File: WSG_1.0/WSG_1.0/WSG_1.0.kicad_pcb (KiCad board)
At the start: 4 copper layers, 53.8 x 34.1 mm, 100 parts, among them J1 Conn_01x10, J2 USB_C_Receptacle_USB2.0_16P, J4 Conn_01x02, SW1 SW_Push, SW2 SW_Push, U1 ADS131A04IPBSR, U10 TPS22916CYFPR, U11 W25N04KVZEIR, U12 USBLC6-2SC6, U13 ESP32-S3-MINI-1-N8, U14 TPD4E1U06DBVR, U2 DAC60501ZDGSR, U3 INA827AIDGKR, U4 INA827AIDGKR, U5 INA827AIDGKR, U6 TMP235A2DBZR, U7 BQ25180YBGR, U8 TPS63802DLAR, U9 TPS7A2025PDBVR, Y1 SiT8008AI-13-33S-16.384000

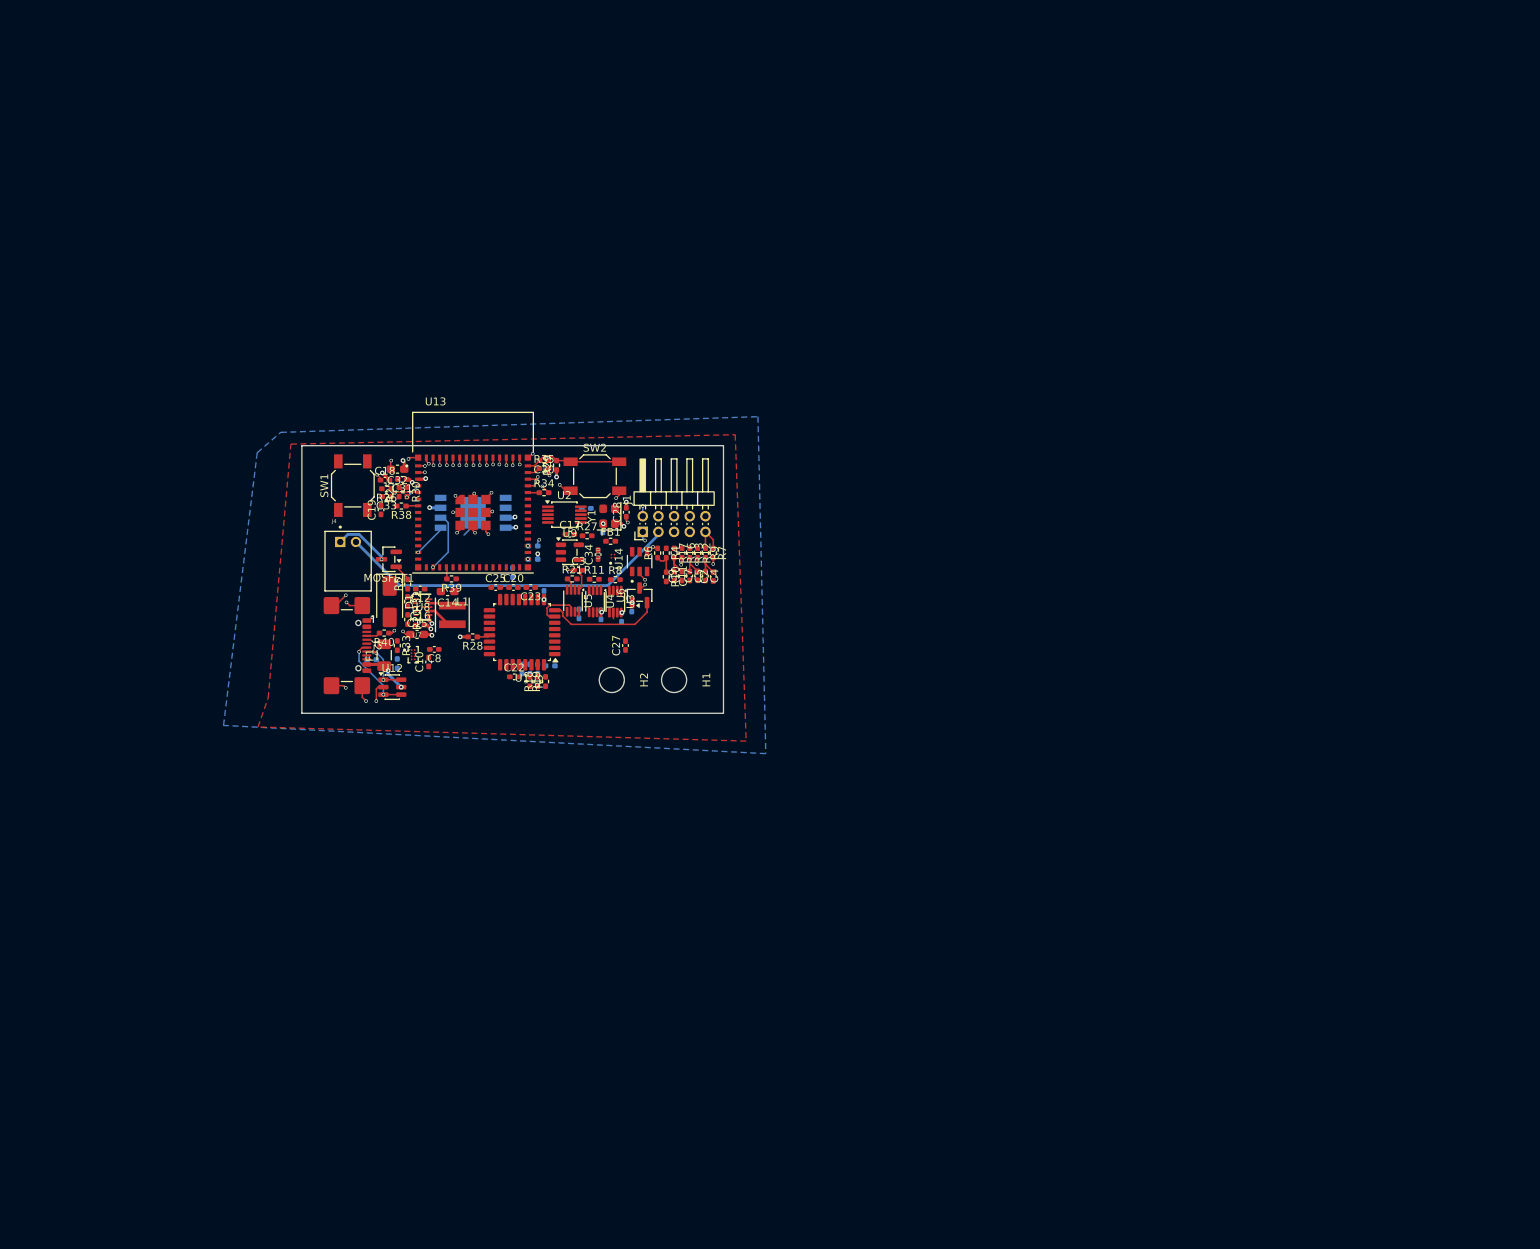
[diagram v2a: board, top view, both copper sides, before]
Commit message: new layout started, clusters almost done
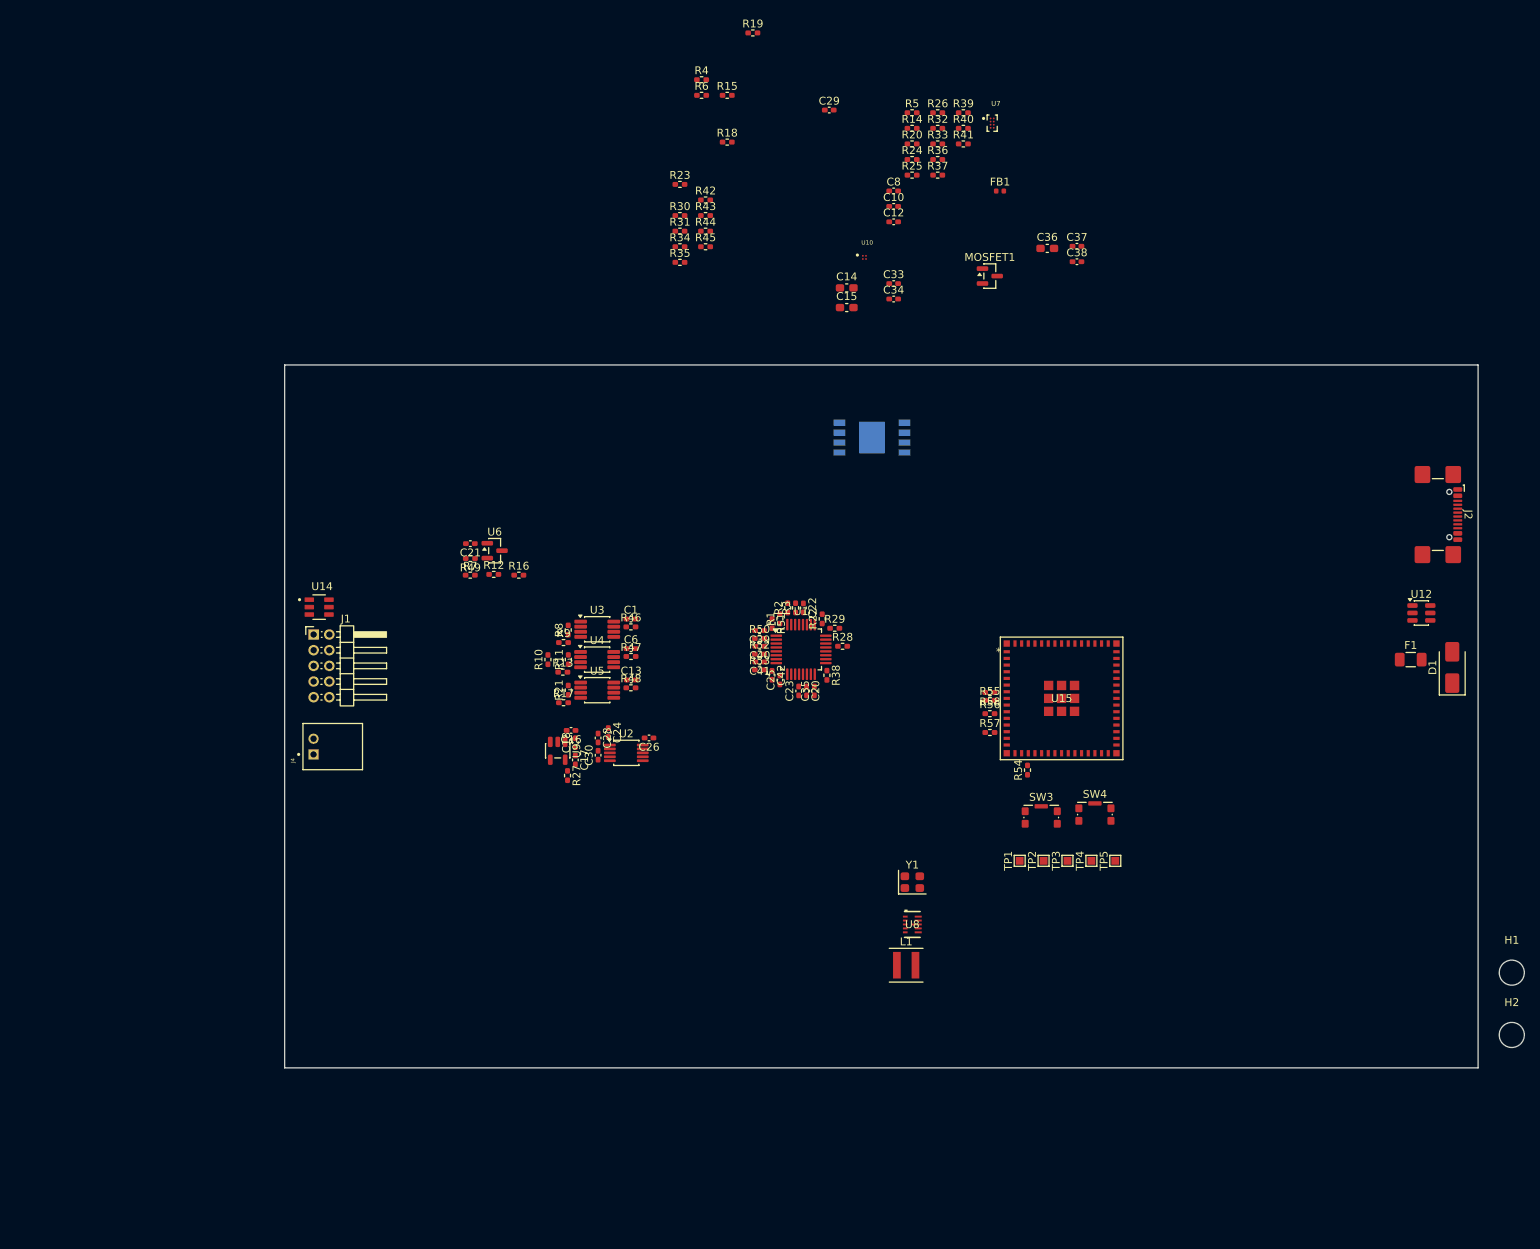
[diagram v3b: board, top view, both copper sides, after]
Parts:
- removed C11, C27, C31, C4, C5: 0.1uF, Capacitor_SMD:C_0402_1005Metric_Pad0.74x0.62mm_HandSolder
- removed C19: 100nF, Capacitor_SMD:C_0402_1005Metric_Pad0.74x0.62mm_HandSolder
- removed C2, C3, C7, C9: 10nF, Capacitor_SMD:C_0402_1005Metric_Pad0.74x0.62mm_HandSolder
- removed C32: 22uF, Capacitor_SMD:C_0603_1608Metric_Pad1.08x0.95mm_HandSolder
- removed SW1, SW2: SW_Push, Button_Switch_SMD:SW_SPST_SKQG_WithStem
- removed U13: ESP32-S3-MINI-1-N8, footprints:XCVR_ESP32-S3-MINI-1-N8
- added C36: 22uF, Capacitor_SMD:C_0603_1608Metric_Pad1.08x0.95mm_HandSolder, F.Cu at (183.6, 46.5)
- added C37: 0.1uF, Capacitor_SMD:C_0402_1005Metric_Pad0.74x0.62mm_HandSolder, F.Cu at (187.4, 46.3)
- added C38: 1uF, Capacitor_SMD:C_0402_1005Metric_Pad0.74x0.62mm_HandSolder, F.Cu at (187.4, 48.2)
- added C39: 2.7nF, Capacitor_SMD:C_0402_1005Metric_Pad0.74x0.62mm_HandSolder, F.Cu at (146.9, 95.3)
- added C40: 2.7nF, Capacitor_SMD:C_0402_1005Metric_Pad0.74x0.62mm_HandSolder, F.Cu at (146.9, 97.3)
- added C41: 2.7nF, Capacitor_SMD:C_0402_1005Metric_Pad0.74x0.62mm_HandSolder, F.Cu at (146.9, 99.3)
- added C42: 680pF, Capacitor_SMD:C_0402_1005Metric_Pad0.74x0.62mm_HandSolder, F.Cu at (148.5, 101.0)
- added R22: 50, Resistor_SMD:R_0402_1005Metric_Pad0.72x0.64mm_HandSolder, F.Cu at (154.9, 93.8)
- added R23: 100k, Resistor_SMD:R_0402_1005Metric_Pad0.72x0.64mm_HandSolder, F.Cu at (136.7, 38.4)
- added R31: 10k, Resistor_SMD:R_0402_1005Metric_Pad0.72x0.64mm_HandSolder, F.Cu at (136.7, 44.3)
- added R42: 10k, Resistor_SMD:R_0402_1005Metric_Pad0.72x0.64mm_HandSolder, F.Cu at (140.0, 40.3)
- added R43: 10k, Resistor_SMD:R_0402_1005Metric_Pad0.72x0.64mm_HandSolder, F.Cu at (140.0, 42.3)
- added R44: 10k, Resistor_SMD:R_0402_1005Metric_Pad0.72x0.64mm_HandSolder, F.Cu at (140.0, 44.3)
- added R45: 10k, Resistor_SMD:R_0402_1005Metric_Pad0.72x0.64mm_HandSolder, F.Cu at (140.0, 46.3)
- added R46: 100, Resistor_SMD:R_0402_1005Metric_Pad0.72x0.64mm_HandSolder, F.Cu at (130.5, 94.8)
- added R47: 100, Resistor_SMD:R_0402_1005Metric_Pad0.72x0.64mm_HandSolder, F.Cu at (130.5, 98.6)
- added R48: 100, Resistor_SMD:R_0402_1005Metric_Pad0.72x0.64mm_HandSolder, F.Cu at (130.5, 102.6)
- added R49: 100, Resistor_SMD:R_0402_1005Metric_Pad0.72x0.64mm_HandSolder, F.Cu at (110.0, 86.1)
- added R50: 100, Resistor_SMD:R_0402_1005Metric_Pad0.72x0.64mm_HandSolder, F.Cu at (146.9, 96.3)
- added R51: 100, Resistor_SMD:R_0402_1005Metric_Pad0.72x0.64mm_HandSolder, F.Cu at (148.5, 94.4)
- added R52: 100, Resistor_SMD:R_0402_1005Metric_Pad0.72x0.64mm_HandSolder, F.Cu at (146.9, 98.3)
- added R53: 100, Resistor_SMD:R_0402_1005Metric_Pad0.72x0.64mm_HandSolder, F.Cu at (146.9, 100.3)
- added R54: 1k, Resistor_SMD:R_0402_1005Metric_Pad0.72x0.64mm_HandSolder, F.Cu at (181.1, 113.1)
- added R55: 1k, Resistor_SMD:R_0402_1005Metric_Pad0.72x0.64mm_HandSolder, F.Cu at (176.3, 104.2)
- added R56: 1k, Resistor_SMD:R_0402_1005Metric_Pad0.72x0.64mm_HandSolder, F.Cu at (176.3, 105.9)
- added R57: 1k, Resistor_SMD:R_0402_1005Metric_Pad0.72x0.64mm_HandSolder, F.Cu at (176.3, 108.3)
- added R58: 1k, Resistor_SMD:R_0402_1005Metric_Pad0.72x0.64mm_HandSolder, F.Cu at (176.3, 103.2)
- added SW3: SW_Push, Button_Switch_SMD:SW_SPST_CK_KMS2xxG, F.Cu at (182.8, 119.2)
- added SW4: SW_Push, Button_Switch_SMD:SW_SPST_CK_KMS2xxG, F.Cu at (189.7, 118.8)
- added TP1: TestPoint, TestPoint:TestPoint_Pad_1.0x1.0mm, F.Cu at (180.1, 124.7)
- added TP2: TestPoint, TestPoint:TestPoint_Pad_1.0x1.0mm, F.Cu at (183.2, 124.7)
- added TP3: TestPoint, TestPoint:TestPoint_Pad_1.0x1.0mm, F.Cu at (186.2, 124.7)
- added TP4: TestPoint, TestPoint:TestPoint_Pad_1.0x1.0mm, F.Cu at (189.2, 124.7)
- added TP5: TestPoint, TestPoint:TestPoint_Pad_1.0x1.0mm, F.Cu at (192.3, 124.7)
- added U15: ESP32-S3-MINI-1U-N8, footprints:ESP32-S3-MINI-1U_EXP, F.Cu at (185.4, 104.0)
- C1, C13, C21, C24, C26, C29, C35, C6, R1, R14, R15, R2, R24, R36, R37, R41: moved to F.Cu
- C30: value 1uF -> 1nF
- FB1: value 0 -> 600R@100MHz; footprint Resistor_SMD:R_0402_1005Metric_Pad0.72x0.64mm_HandSolder -> Inductor_SMD:L_0402_1005Metric
- MOSFET1: value DMP2035U-7 -> AO3401A
- R29, R30, R38: value 10k -> 100k
- R34, R35: value 10k -> 22
- U1: footprint Package_QFP:TQFP-32_7x7mm_P0.8mm -> Package_QFP:TQFP-32_5x5mm_P0.5mm
- U3, U4, U5: footprint Package_SO:VSSOP-8_2.3x2mm_P0.5mm -> Package_SO:VSSOP-8_3x3mm_P0.65mm
- Y1: value SiT8008AI-13-33S-16.384000 -> SiT8008AI-12-33S-16.384000
- moved J2 140.2 mm to (232.3, 80.5)
- moved D1 135.9 mm to (235.3, 100.0), turned to 90 degrees
- moved U12 131.7 mm to (231.4, 93.0)
- moved F1 131.0 mm to (230.0, 99.0), turned to 0 degrees
- moved H2 123.5 mm to (242.9, 146.9), turned to 0 degrees
- moved H1 113.2 mm to (242.9, 138.9), turned to 0 degrees
- moved U7 100.3 mm to (176.6, 30.5)
- moved R41 100.2 mm to (172.9, 33.2), turned to 0 degrees
- moved R40 98.0 mm to (172.9, 31.2), turned to 0 degrees
- moved R14 94.8 mm to (166.4, 31.2), turned to 0 degrees
- moved R33 94.1 mm to (169.6, 33.2), turned to 0 degrees
- moved R32 90.7 mm to (169.6, 31.2), turned to 0 degrees
- moved R20 88.5 mm to (166.4, 33.2), turned to 0 degrees
- moved R39 88.3 mm to (172.9, 29.2), turned to 0 degrees
- moved R5 88.1 mm to (166.4, 29.2), turned to 0 degrees
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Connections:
- net Net-(U10-VIN) renamed 3V3_F
- C30 pad 2: EN -> VREF_1V65
- R29 pad 1: 3V3 -> ADC_CS
- R29 pad 2: EN -> 3V3A
- R30 pad 1: 3V3 -> DAC_CS
- R30 pad 2: Net-(U13-IO0) -> 3V3A
- R34 pad 1: Net-(U13-IO45) -> USB_DM
- R34 pad 2: GND -> Net-(U15-IO19)
- R35 pad 1: Net-(U13-IO46) -> USB_DP
- R35 pad 2: GND -> Net-(U15-IO20)
- R38 pad 1: Net-(U13-IO3) -> ADC_RST
- R38 pad 2: GND -> 3V3A
- U1 pad 1: VREF_1V65 -> Net-(U1-AIN1N)
- U1 pad 3: VREF_1V65 -> Net-(U1-AIN2N)
- U1 pad 5: VREF_1V65 -> Net-(U1-AIN3N)
- U1 pad 7: VREF_1V65 -> Net-(U1-AIN4N)
- U3 pad 7: AIN0P -> Net-(U3-VOUT)
- U4 pad 7: AIN1P -> Net-(U4-VOUT)
- U5 pad 7: AIN2P -> Net-(U5-VOUT)
- U6 pad 2: AIN3P -> Net-(U6-VOUT)
- Y1 pad 3: CLK16M -> Net-(Y1-OUT)
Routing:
- net GND: track 64.6 -> 0.00 mm, vias 55 -> 0
- net BATT_N: track 44.0 -> 0.00 mm
- net AIN3P: track 14.6 -> 0.00 mm
- net 3V3: track 13.3 -> 0.00 mm, vias 12 -> 0
- net EN: track 12.5 -> 0.00 mm
- net USB_DM: track 10.4 -> 0.00 mm, vias 2 -> 0
- net FLASH_MISO: track 7.74 -> 0.00 mm, vias 1 -> 0
- net USB_DP: track 7.44 -> 0.00 mm, vias 2 -> 0
- net VREF_1V65: track 7.24 -> 0.00 mm
- net BATT_P: track 7.16 -> 0.00 mm, vias 1 -> 0
- net VBUS: track 5.89 -> 0.00 mm, vias 2 -> 0
- net SIG0: track 4.62 -> 0.00 mm
- net VBAT_SENSE: track 4.50 -> 0.00 mm
- net FLASH_CS: track 4.34 -> 0.00 mm, vias 1 -> 0
- net INP0: track 4.02 -> 0.00 mm
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- removed copper zone on In2.Cu, net 3V3
- removed copper zone on In2.Cu, net 3V3A
- removed copper zone on B.Cu, net GND
- removed copper zone on F.Cu, net GND
- removed copper zone on In1.Cu, net GND
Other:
- board size 53.8 x 34.1 mm -> 152.3 x 89.7 mm

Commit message: relocated resistors to esp
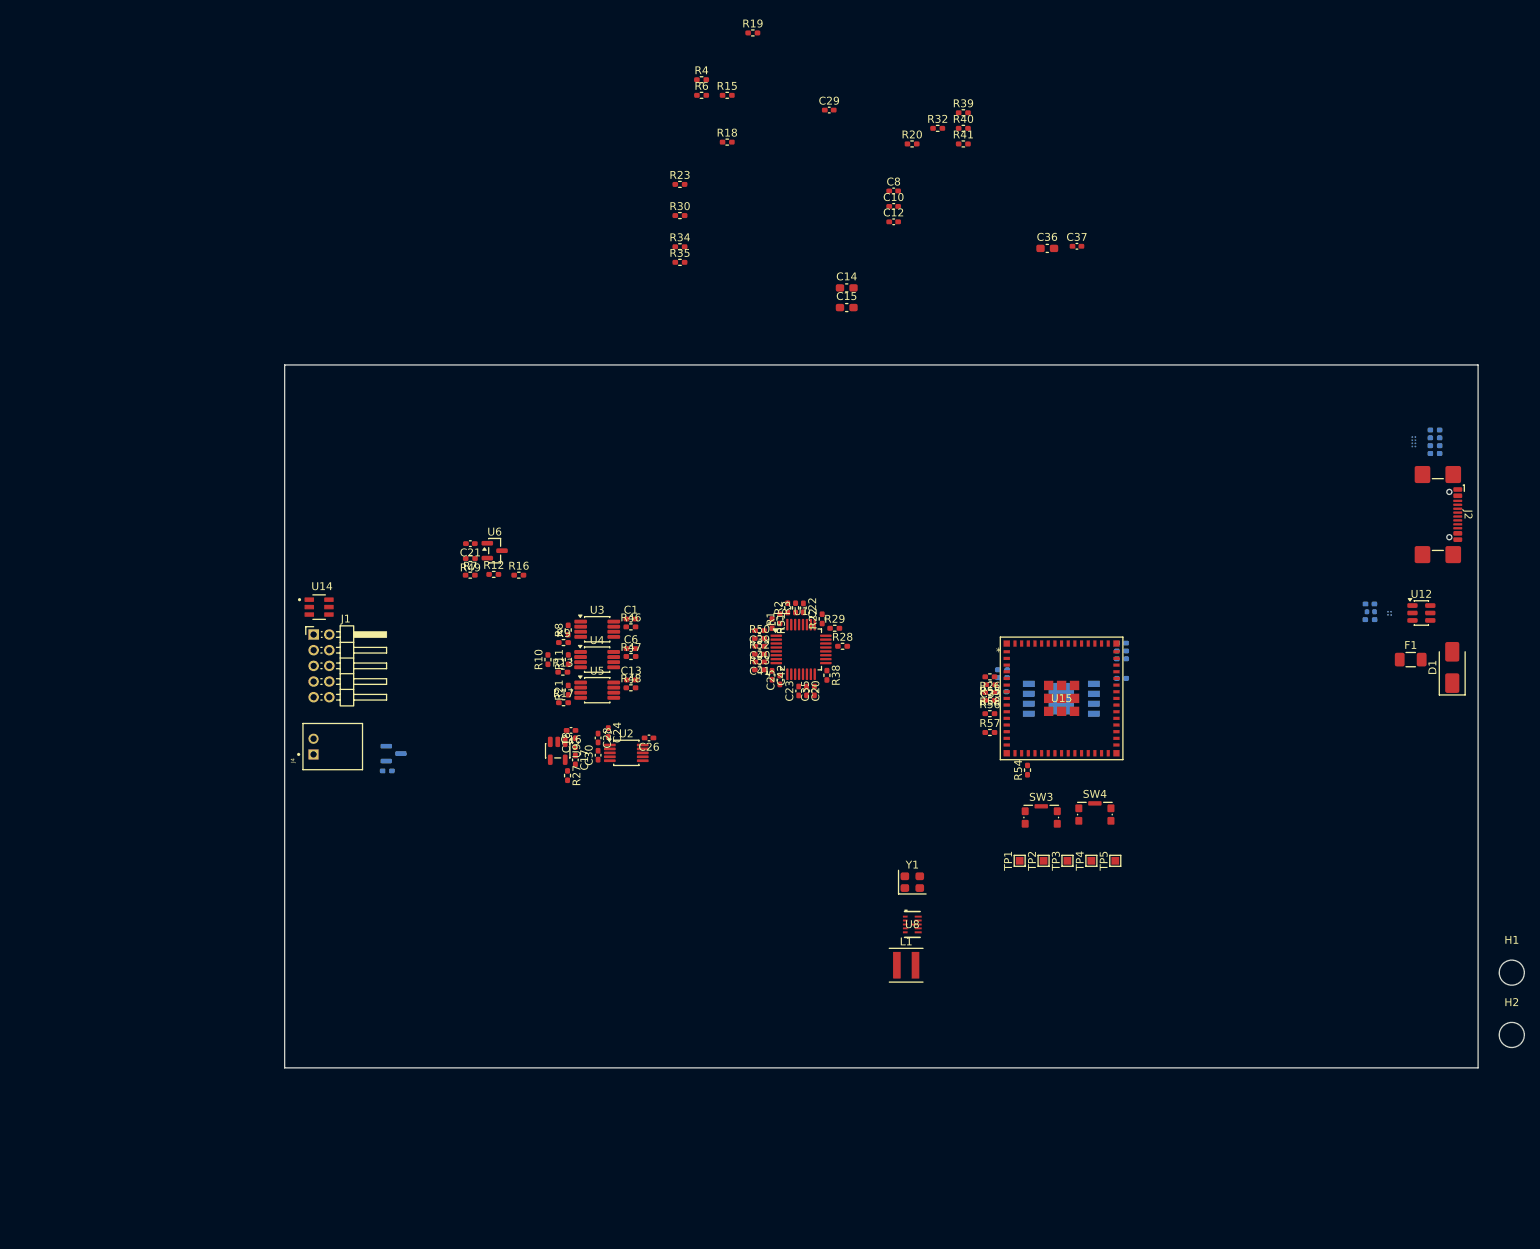
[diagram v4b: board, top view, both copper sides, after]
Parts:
- C34, C38, FB1, MOSFET1, R14, R24, R25, R31, R33, R36, R37, R42, R43, R44, R45, R5, U10, U7: moved to B.Cu
- moved R5 107.4 mm to (99.4, 113.2), turned to 180 degrees
- moved MOSFET1 97.5 mm to (100.2, 111.0)
- moved R24 82.8 mm to (224.8, 93.9), turned to 180 degrees
- moved U10 81.0 mm to (227.3, 93.1), turned to 180 degrees
- moved R43 79.4 mm to (193.1, 101.4)
- moved R14 78.6 mm to (233.1, 72.7)
- moved R44 76.1 mm to (193.1, 98.9)
- moved R45 74.0 mm to (193.1, 97.9), turned to 180 degrees
- moved R42 73.3 mm to (177.8, 103.1), turned to 180 degrees
- moved R36 73.2 mm to (233.1, 71.7), turned to 180 degrees
- moved R33 73.2 mm to (233.1, 69.7), turned to 180 degrees
- moved R26 72.3 mm to (176.3, 101.2), turned to 180 degrees
- moved C34 72.2 mm to (224.8, 91.9)
- moved R37 71.8 mm to (233.1, 70.7), turned to 180 degrees
- moved FB1 71.6 mm to (224.9, 92.9), turned to 180 degrees
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
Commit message: new layout, trying different layout onw
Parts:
- added C2: 1uF, Capacitor_SMD:C_0402_1005Metric_Pad0.74x0.62mm_HandSolder, B.Cu at (128.3, 63.1)
- added C31: 1uF, Capacitor_SMD:C_0402_1005Metric_Pad0.74x0.62mm_HandSolder, F.Cu at (101.5, 68.4)
- C10, C12, C16, C17, C18, C21, C8, F1, R15, R18, R19, R23, R49, U6, U9: moved to B.Cu
- moved C34 102.8 mm to (125.9, 63.8)
- moved FB1 102.8 mm to (126.0, 64.8)
- moved R24 102.8 mm to (125.9, 65.8)
- moved U10 102.8 mm to (128.4, 65.0)
- moved U12 102.8 mm to (132.4, 65.0)
- moved D1 99.5 mm to (142.2, 64.8), turned to 0 degrees
- moved R14 96.2 mm to (137.1, 66.2)
- moved R33 96.2 mm to (137.1, 63.2)
- moved R36 96.2 mm to (137.1, 65.2)
- moved R37 96.2 mm to (137.1, 64.2)
- moved U7 96.2 mm to (134.4, 64.7)
- moved F1 90.3 mm to (145.7, 66.7), turned to 180 degrees
- moved TP5 83.3 mm to (120.5, 82.5)
- moved TP4 82.5 mm to (118.3, 82.5)
- moved J2 82.1 mm to (151.0, 69.1), turned to 90 degrees
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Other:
- board size 152.3 x 89.7 mm -> 68.8 x 27.7 mm
